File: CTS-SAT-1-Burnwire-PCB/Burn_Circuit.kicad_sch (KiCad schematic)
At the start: 7 parts, among them Q1 AO3400A

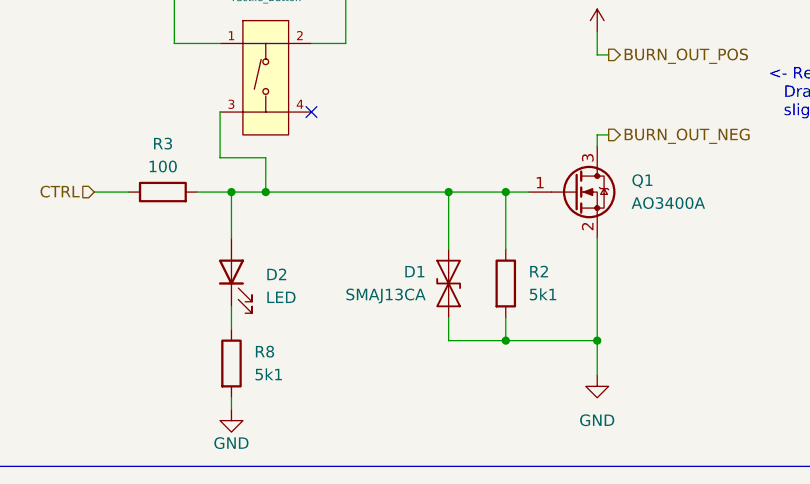
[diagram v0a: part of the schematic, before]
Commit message: Replace TVS diodes with SMAJ6.5CA
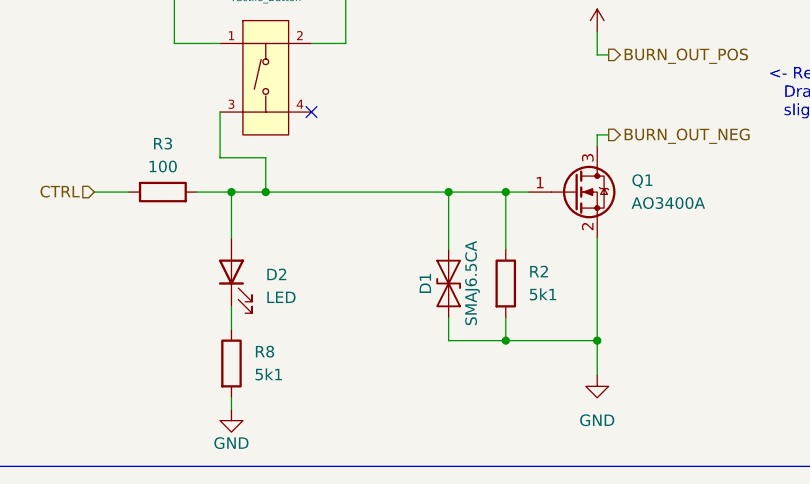
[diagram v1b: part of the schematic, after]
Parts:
- D1: value SMAJ13CA -> SMAJ6.5CA; symbol Diode:SMAJ13CA -> Diode:SMAJ6.5CA
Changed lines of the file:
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@@
 	)
 	(symbol
-		(lib_id "Diode:SMAJ13CA")
+		(lib_id "Diode:SMAJ6.5CA")
 		(at 106.68 83.82 90)
 		(unit 1)
@@
 		(dnp no)
 		(property "Reference" "D1"
-			(at 104.14 82.5499 90)
+			(at 104.14 83.82 0)
 			(effects
 				(font
 					(size 1.27 1.27)
 				)
-				(justify left)
 			)
 		)
-		(property "Value" "SMAJ13CA"
-			(at 104.14 85.0899 90)
+		(property "Value" "SMAJ6.5CA"
+			(at 109.22 83.82 0)
 			(effects
 				(font
 					(size 1.27 1.27)
 				)
-				(justify left)
 			)
 		)
@@
 			)
 		)
-		(property "Description" "400W bidirectional Transient Voltage Suppressor, 13.0Vr, SMA(DO-214AC)"
+		(property "Description" "400W bidirectional Transient Voltage Suppressor, 6.5Vr, SMA(DO-214AC)"
 			(at 106.68 83.82 0)
 			(effects

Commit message: Bump version number, add renders, clean up vias through silkscreens
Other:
- title: (none) -> CTS-SAT-1 DCLB Burn Wire PCB
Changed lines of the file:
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@@
 	(generator "eeschema")
 	(generator_version "9.0")
-	(paper "A4")
+	(paper "USLetter")
+	(title_block
+		(title "CTS-SAT-1 DCLB Burn Wire PCB")
+		(date "2025-05-08")
+		(rev "Rev 2")
+	)
 	(rectangle
 		(start 49.53 33.02)

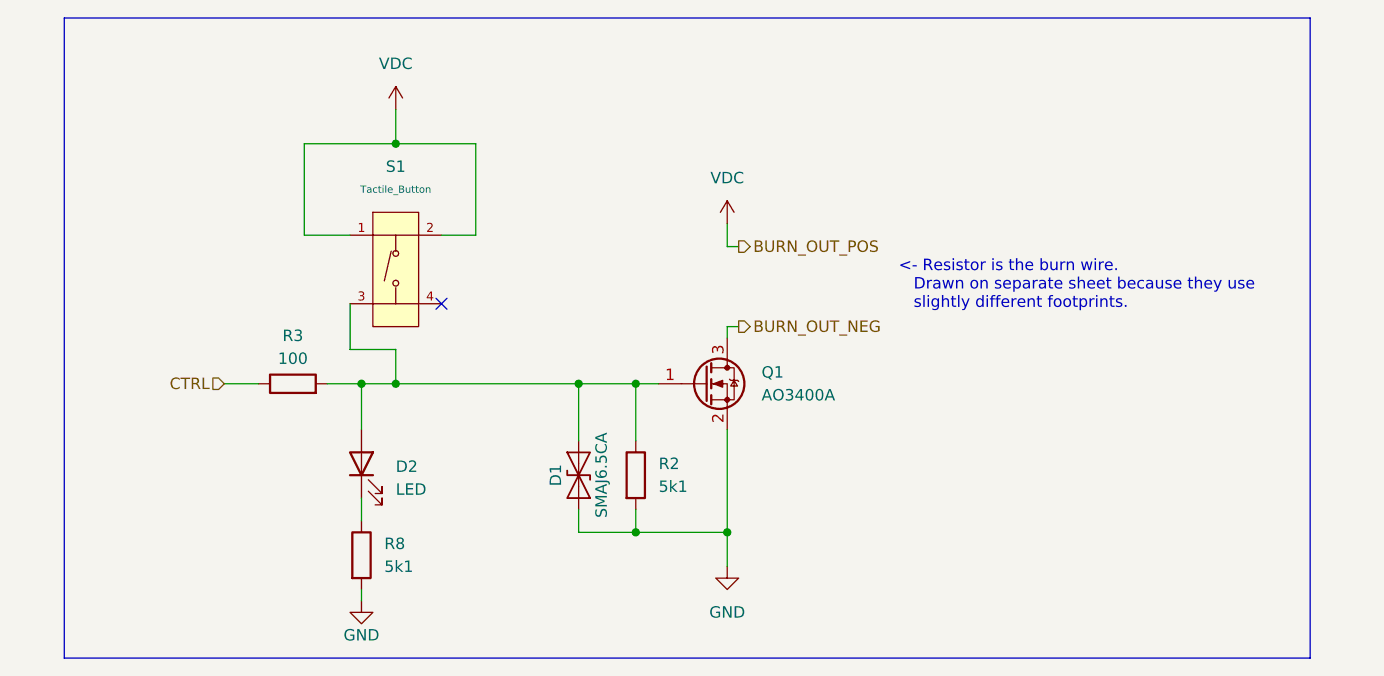
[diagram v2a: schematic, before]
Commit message: Update part numbers in schematic
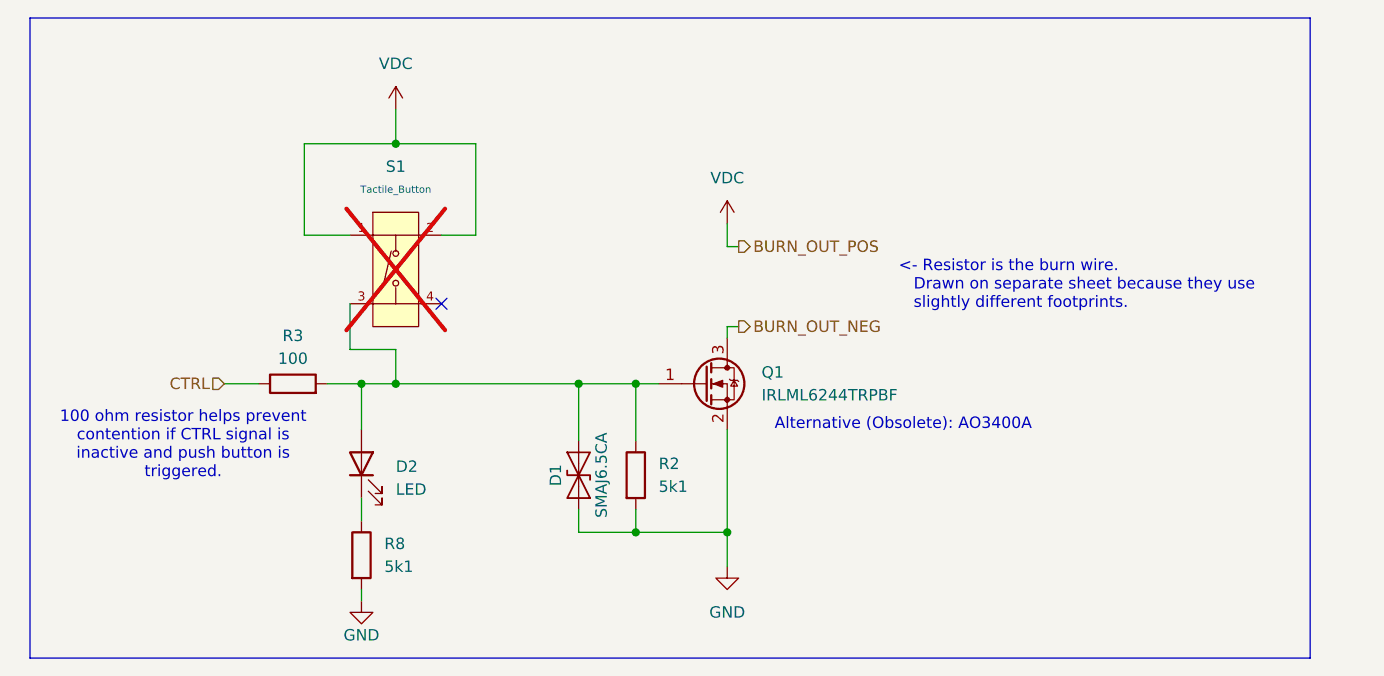
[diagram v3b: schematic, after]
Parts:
- Q1: value AO3400A -> IRLML6244TRPBF
- S1: now not fitted
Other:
- note added: "100 ohm resistor helps prevent contention if CTRL signal is inactive and push button is triggered."
- note added: "Alternative (Obsolete): AO3400A"
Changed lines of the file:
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@@
 	)
 	(rectangle
-		(start 49.53 33.02)
+		(start 45.72 33.02)
 		(end 187.96 104.14)
 		(stroke
@@
 		(fill
 			(type none)
+		)
+	)
+	(text "100 ohm resistor helps prevent\ncontention if CTRL signal is \ninactive and push button is\ntriggered."
+		(exclude_from_sim no)
+		(at 62.738 80.518 0)
+		(effects
+			(font
+				(size 1.27 1.27)
+			)
+		)
+	)
+	(text "Alternative (Obsolete): AO3400A"
+		(exclude_from_sim no)
+		(at 142.748 78.232 0)
+		(effects
+			(font
+				(size 1.27 1.27)
+			)
 		)
 	)
@@
 			)
 		)
-		(property "Value" "AO3400A"
+		(property "Value" "IRLML6244TRPBF"
 			(at 127 74.9299 0)
 			(effects
@@
 		(in_bom yes)
 		(on_board yes)
-		(dnp no)
+		(dnp yes)
 		(fields_autoplaced yes)
 		(property "Reference" "S1"
